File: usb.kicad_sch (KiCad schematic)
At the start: 11 parts, among them J1 USB_C, U15 TVS_USB, U29 HUSB238

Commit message: Tune mixer output bias and balun
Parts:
- R106: footprint Resistor_SMD:R_0402_1005Metric -> Resistor_SMD:R_0201_0603Metric; Part Number RC0402JR-0733RL -> RC0201JR-0733RL
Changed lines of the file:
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@@
 			)
 		)
-		(property "Footprint" "Resistor_SMD:R_0402_1005Metric"
+		(property "Footprint" "Resistor_SMD:R_0201_0603Metric"
 			(at 139.7 48.26 0)
 			(effects
@@
 			)
 		)
-		(property "Description" "RES 33 OHM 5% 1/16W 0402"
+		(property "Description" "RES 33 OHM 5% 1/20W 0201"
 			(at 139.7 48.26 0)
 			(effects
@@
 			)
 		)
-		(property "Part Number" "RC0402JR-0733RL"
+		(property "Part Number" "RC0201JR-0733RL"
 			(at 139.7 48.26 0)
 			(effects

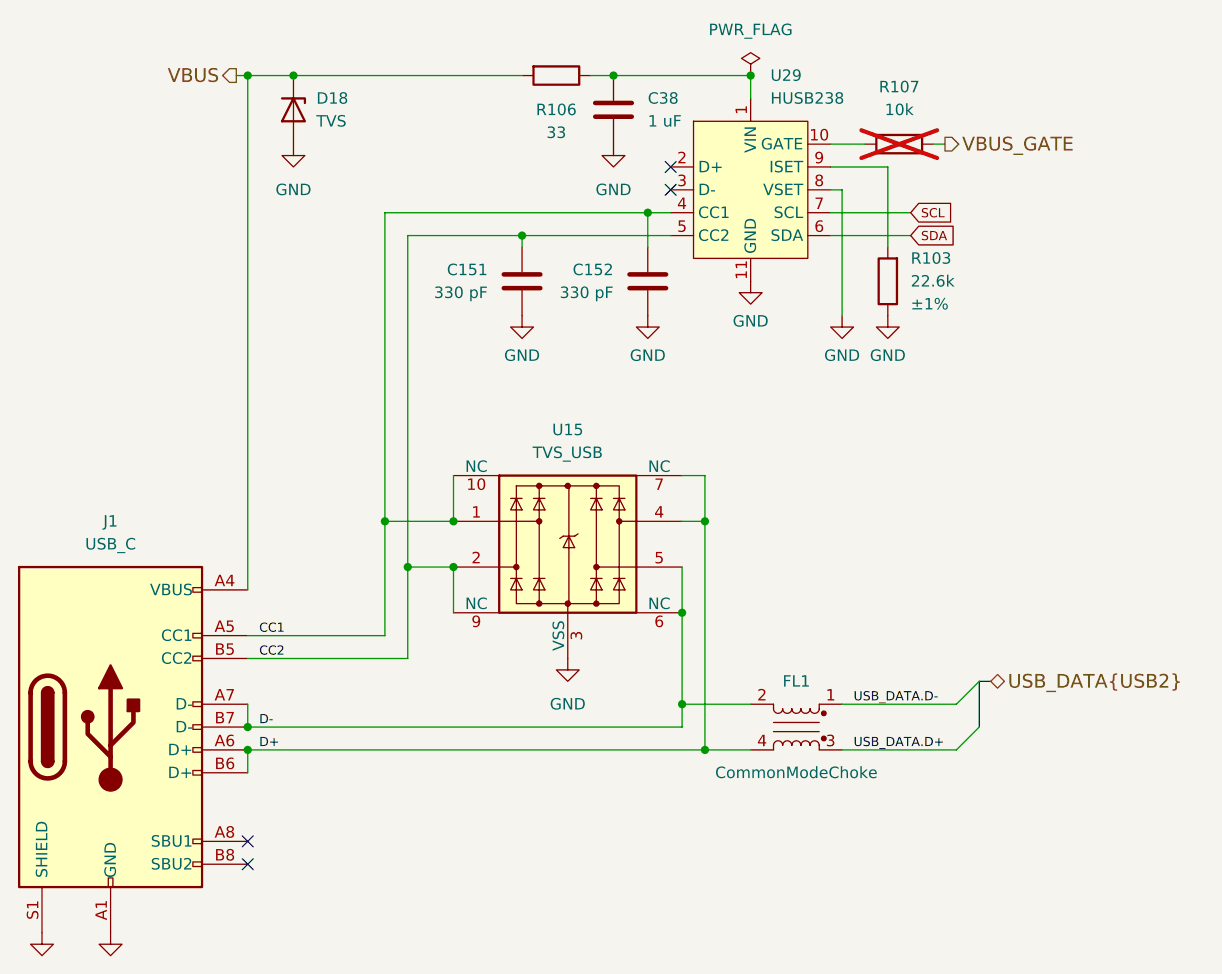
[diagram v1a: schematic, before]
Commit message: Use Type-C power instead of Type-C controller
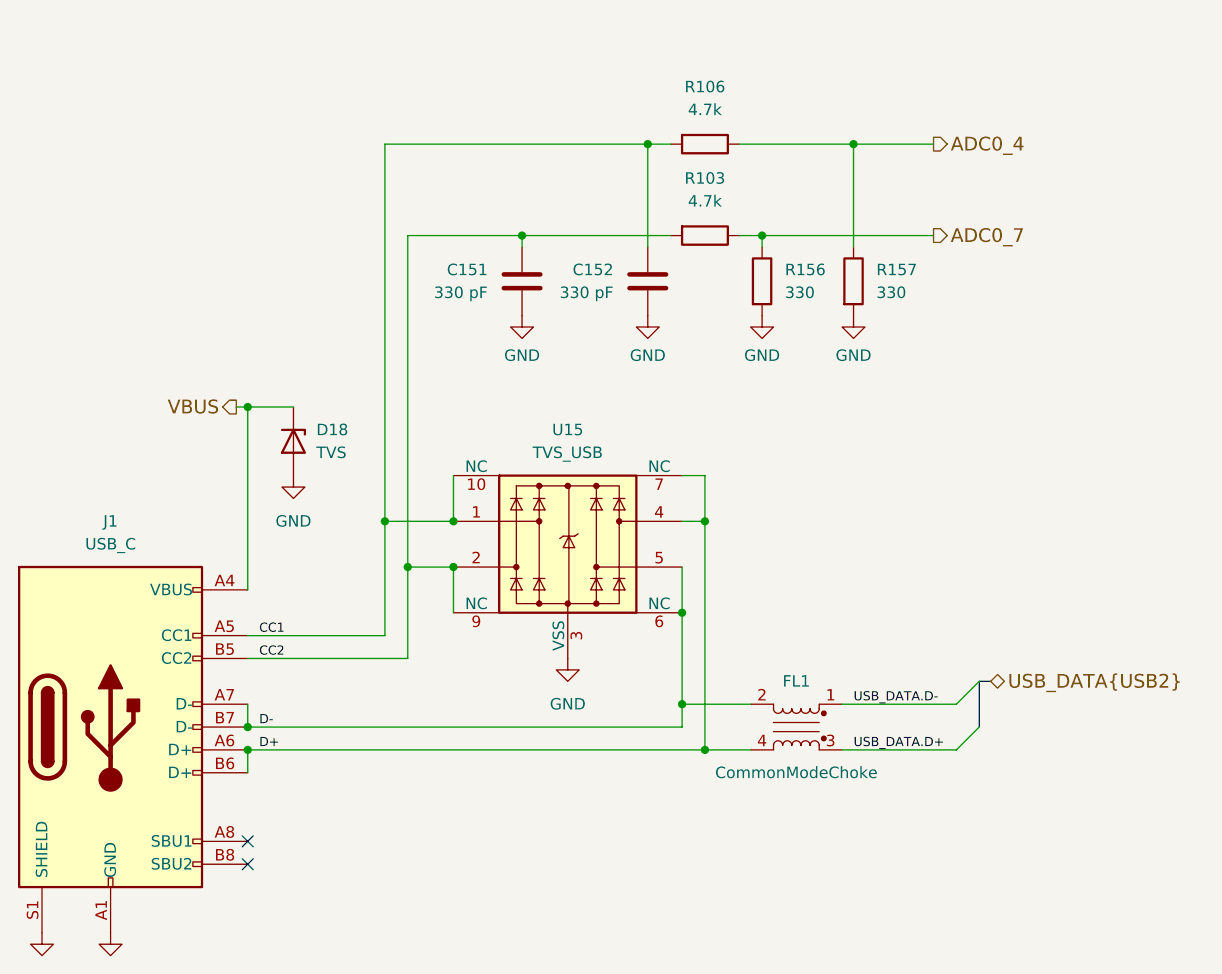
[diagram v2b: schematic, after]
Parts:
- removed C38: 1 uF, Capacitor_SMD:C_0402_1005Metric, symbol Device:C
- removed R107: 10k, Resistor_SMD:R_0402_1005Metric, symbol Device:R
- removed U29: HUSB238, praline:WDFN-10-1EP_3x3mm_P0.5mm_EP1.8x2.5mm_ThermalVias, symbol praline:HUSB238
- added R156, R157: 330, Resistor_SMD:R_0201_0603Metric, symbol Device:R
- R103: value 22.6k -> 4.7k; Part Number RC0201FR-0722K6L -> RC0201FR-074K7L; Tolerance ±1% -> (none)
- R106: value 33 -> 4.7k; Part Number RC0201JR-0733RL -> RC0201FR-074K7L
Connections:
- net CC1: now also R106.2
- net CC2: now also R103.2
- net GND: now also R156.2, R157.2; no longer R103.1
- net VBUS: no longer R106.2
- net ADC0_4: now reaches R106.1
- net ADC0_4: now also R157.1
- new net ADC0_7: R103.1, R156.1
- no-connect marks 4 -> 2
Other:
- moved on the sheet: D18
